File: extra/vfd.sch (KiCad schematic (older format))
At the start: 47 parts, among them P10 GU128x64E-U100, P11 gui140x16j-7002, P12 digital_in, P13 digital_out, U3 74LS125, U4 74LS125, U5 74LS125, U6 74LS125, U7 74LS125, U8 74LS245-xnor

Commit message: working with enables on extra board
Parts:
- added R? (x3): PULL, xnorman:Resistor_Horizontal_RM10mm-xnorman, symbol R
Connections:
- net 3.3v: now also R?.1
- net GND: no longer U3.1 (E), U3.10 (E), U3.13 (E), U3.4 (E), U4.1 (E), U4.10 (E), U4.4 (E), U5.1 (E), U5.10 (E), U5.13 (E), U5.4 (E), U7.13 (E), U8.19 (CE)
- net VCC: now also R?.2, R?.2
- net bb-vfdD7enable renamed bb-vfdDOUTenable
- net bb-vfdDOUTenable: now also U3.1 (E), U3.10 (E), U3.13 (E), U3.4 (E), U4.1 (E), U4.10 (E), U4.4 (E), R?.1
- new net bb-digitalOutEnable: U8.19 (CE)
- new net bb-vfdCTRLenable: R?.1, U5.1 (E), U5.10 (E), U5.13 (E), U5.4 (E), U7.13 (E)
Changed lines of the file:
@@
 $Descr A4 11693 8268
 encoding utf-8
-Sheet 3 2
+Sheet 2 2
 Title ""
 Date ""
@@
 $EndComp
 Text GLabel 1250 7650 0    60   Input ~ 0
-bb-vfdD7enable
+bb-vfdDOUTenable
 $Comp
 L 74LS125 U5
@@
 Wire Wire Line
 	1750 1250 2200 1250
-Connection ~ 2050 1250
 Wire Wire Line
 	1250 850  1150 850
@@
 	2150 7250 2350 7250
 Wire Wire Line
-	1350 3600 1700 3600
-Wire Wire Line
-	1350 4150 1700 4150
-Wire Wire Line
-	1350 4750 1700 4750
-Wire Wire Line
-	1350 5250 1700 5250
-Wire Wire Line
-	1350 5900 1700 5900
-Wire Wire Line
-	1350 6450 1700 6450
-Wire Wire Line
-	1350 7050 1700 7050
-Wire Wire Line
-	1250 7650 1700 7650
-Wire Wire Line
 	1700 7650 1700 7550
 Wire Wire Line
@@
 	6050 4850 6250 4850
 Wire Wire Line
-	5200 3500 5600 3500
-Wire Wire Line
-	5200 4050 5600 4050
-Wire Wire Line
-	5200 4650 5600 4650
-Wire Wire Line
-	5200 5150 5600 5150
-Wire Wire Line
 	6250 5500 6050 5500
 Wire Wire Line
@@
 	8700 2000 8950 2000
 Wire Wire Line
-	8950 2300 8850 2300
+	8750 2300 8950 2300
 Wire Wire Line
 	8150 2450 9650 2450
@@
 Wire Wire Line
 	1500 3450 1550 3450
-Connection ~ 1500 3600
 Wire Wire Line
 	1500 4150 1500 4000
 Wire Wire Line
 	1500 4000 1550 4000
-Connection ~ 1500 4150
 Wire Wire Line
 	1500 4750 1500 4600
 Wire Wire Line
 	1500 4600 1550 4600
-Connection ~ 1500 4750
 Wire Wire Line
 	1500 5250 1500 5100
 Wire Wire Line
 	1500 5100 1550 5100
-Connection ~ 1500 5250
 Wire Wire Line
 	1500 5900 1500 5750
 Wire Wire Line
 	1500 5750 1550 5750
-Connection ~ 1500 5900
 Wire Wire Line
 	1500 6450 1500 6300
 Wire Wire Line
 	1500 6300 1550 6300
-Connection ~ 1500 6450
 Wire Wire Line
 	1500 6900 1500 7400
 Wire Wire Line
 	1500 6900 1550 6900
-Connection ~ 1500 7050
 Wire Wire Line
 	1500 7400 1550 7400
@@
 Connection ~ 1400 6600
 Wire Wire Line
-	5400 3500 5400 3350
-Wire Wire Line
 	5400 3350 5450 3350
-Connection ~ 5400 3500
 Wire Wire Line
 	5400 4050 5400 3900
 Wire Wire Line
 	5400 3900 5450 3900
-Connection ~ 5400 4050
 Wire Wire Line
 	5400 4650 5400 4500
 Wire Wire Line
 	5400 4500 5450 4500
-Connection ~ 5400 4650
 Wire Wire Line
 	5400 5150 5400 5000
 Wire Wire Line
 	5400 5000 5450 5000
-Connection ~ 5400 5150
 Wire Wire Line
 	5400 5800 5400 5650
@@
 	8800 5950 9200 5950
 Wire Wire Line
-	8800 6450 9200 6450
+	8800 6450 9000 6450
 Wire Wire Line
 	8550 4500 8750 4500
@@
 Wire Wire Line
 	9000 6300 9050 6300
-Connection ~ 9000 6450
 Wire Wire Line
 	8950 6000 9050 6000
@@
 Wire Wire Line
 	4900 2300 5400 2300
-Connection ~ 8850 2300
 $Comp
 L CONN_01X07 P12
@@
 	8150 1900 8150 2450
 Wire Wire Line
-	8850 2300 8850 2450
-Connection ~ 8850 2450
-Wire Wire Line
 	9650 1050 9650 1250
 NoConn ~ 10350 1900
@@
 Wire Wire Line
 	9450 2850 9450 3150
+Wire Wire Line
+	1500 3600 1350 3600
+Wire Wire Line
+	1500 4150 1350 4150
+Wire Wire Line
+	1500 4750 1350 4750
+Wire Wire Line
+	1500 5250 1350 5250
+Wire Wire Line
+	1500 7050 1350 7050
+Connection ~ 1500 7050
+Wire Wire Line
+	1500 6450 1350 6450
+Wire Wire Line
+	1500 5900 1350 5900
+Wire Wire Line
+	1700 3600 2200 3600
+Wire Wire Line
+	2200 3600 2200 7650
+Wire Wire Line
+	2200 4150 1700 4150
+Wire Wire Line
+	2200 4750 1700 4750
+Connection ~ 2200 4150
+Wire Wire Line
+	2200 5250 1700 5250
+Connection ~ 2200 4750
+Wire Wire Line
+	2200 5900 1700 5900
+Connection ~ 2200 5250
+Wire Wire Line
+	2200 6450 1700 6450
+Connection ~ 2200 5900
+Wire Wire Line
+	2200 7050 1700 7050
+Connection ~ 2200 6450
+Wire Wire Line
+	2200 7650 1250 7650
+Connection ~ 2200 7050
+Connection ~ 1700 7650
+Wire Wire Line
+	5400 3500 5400 3350
+Wire Wire Line
+	5400 3500 5200 3500
+Wire Wire Line
+	5400 4050 5200 4050
+Wire Wire Line
+	5400 4650 5200 4650
+Wire Wire Line
+	5400 5150 5200 5150
+Wire Wire Line
+	5600 3500 6100 3500
+Wire Wire Line
+	6100 3500 6100 5150
+Wire Wire Line
+	6100 4050 5600 4050
+Wire Wire Line
+	6100 4650 5600 4650
+Connection ~ 6100 4050
+Wire Wire Line
+	5600 5150 6350 5150
+Connection ~ 6100 4650
+Text GLabel 6350 5150 2    60   Input ~ 0
+bb-vfdCTRLenable
+Connection ~ 6100 5150
+Text GLabel 9350 6450 2    60   Input ~ 0
+bb-vfdCTRLenable
+Wire Wire Line
+	9350 6450 9200 6450
+Text GLabel 8700 2350 0    60   Input ~ 0
+bb-digitalOutEnable
+Wire Wire Line
+	8700 2350 8750 2350
+Wire Wire Line
+	8750 2350 8750 2300
+$Comp
+L R R?
+U 1 1 589BE25B
+P 8900 2450
+F 0 "R?" V 8980 2450 50  0000 C CNN
+F 1 "PULL" V 8900 2450 50  0000 C CNN
+F 2 "xnorman:Resistor_Horizontal_RM10mm-xnorman" V 8830 2450 50  0001 C CNN
+F 3 "" H 8900 2450 50  0000 C CNN
+	1    8900 2450
+	-1   0    0    1
+$EndComp
+Text GLabel 8850 2600 0    60   Input ~ 0
+3.3v
+Wire Wire Line
+	8900 2600 8850 2600
+$Comp
+L R R?
+U 1 1 589BE85D
+P 2500 6550
+F 0 "R?" V 2580 6550 50  0000 C CNN
+F 1 "PULL" V 2500 6550 50  0000 C CNN
+F 2 "xnorman:Resistor_Horizontal_RM10mm-xnorman" V 2430 6550 50  0001 C CNN
+F 3 "" H 2500 6550 50  0000 C CNN
+	1    2500 6550
+	0    -1   -1   0
+$EndComp
+Text GLabel 2800 6550 2    60   Input ~ 0
+5v
+Wire Wire Line
+	2800 6550 2650 6550
+Wire Wire Line
+	2350 6550 2200 6550
+Connection ~ 2200 6550
+$Comp
+L R R?
+U 1 1 589BFAF3
+P 6800 5000
+F 0 "R?" V 6880 5000 50  0000 C CNN
+F 1 "PULL" V 6800 5000 50  0000 C CNN
+F 2 "xnorman:Resistor_Horizontal_RM10mm-xnorman" V 6730 5000 50  0001 C CNN
+F 3 "" H 6800 5000 50  0000 C CNN
+	1    6800 5000
+	0    -1   -1   0
+$EndComp
+Text GLabel 7150 5000 2    60   Input ~ 0
+5v
+Wire Wire Line
+	6650 5000 6100 5000
+Connection ~ 6100 5000
+Wire Wire Line
+	6950 5000 7150 5000
 $EndSCHEMATC

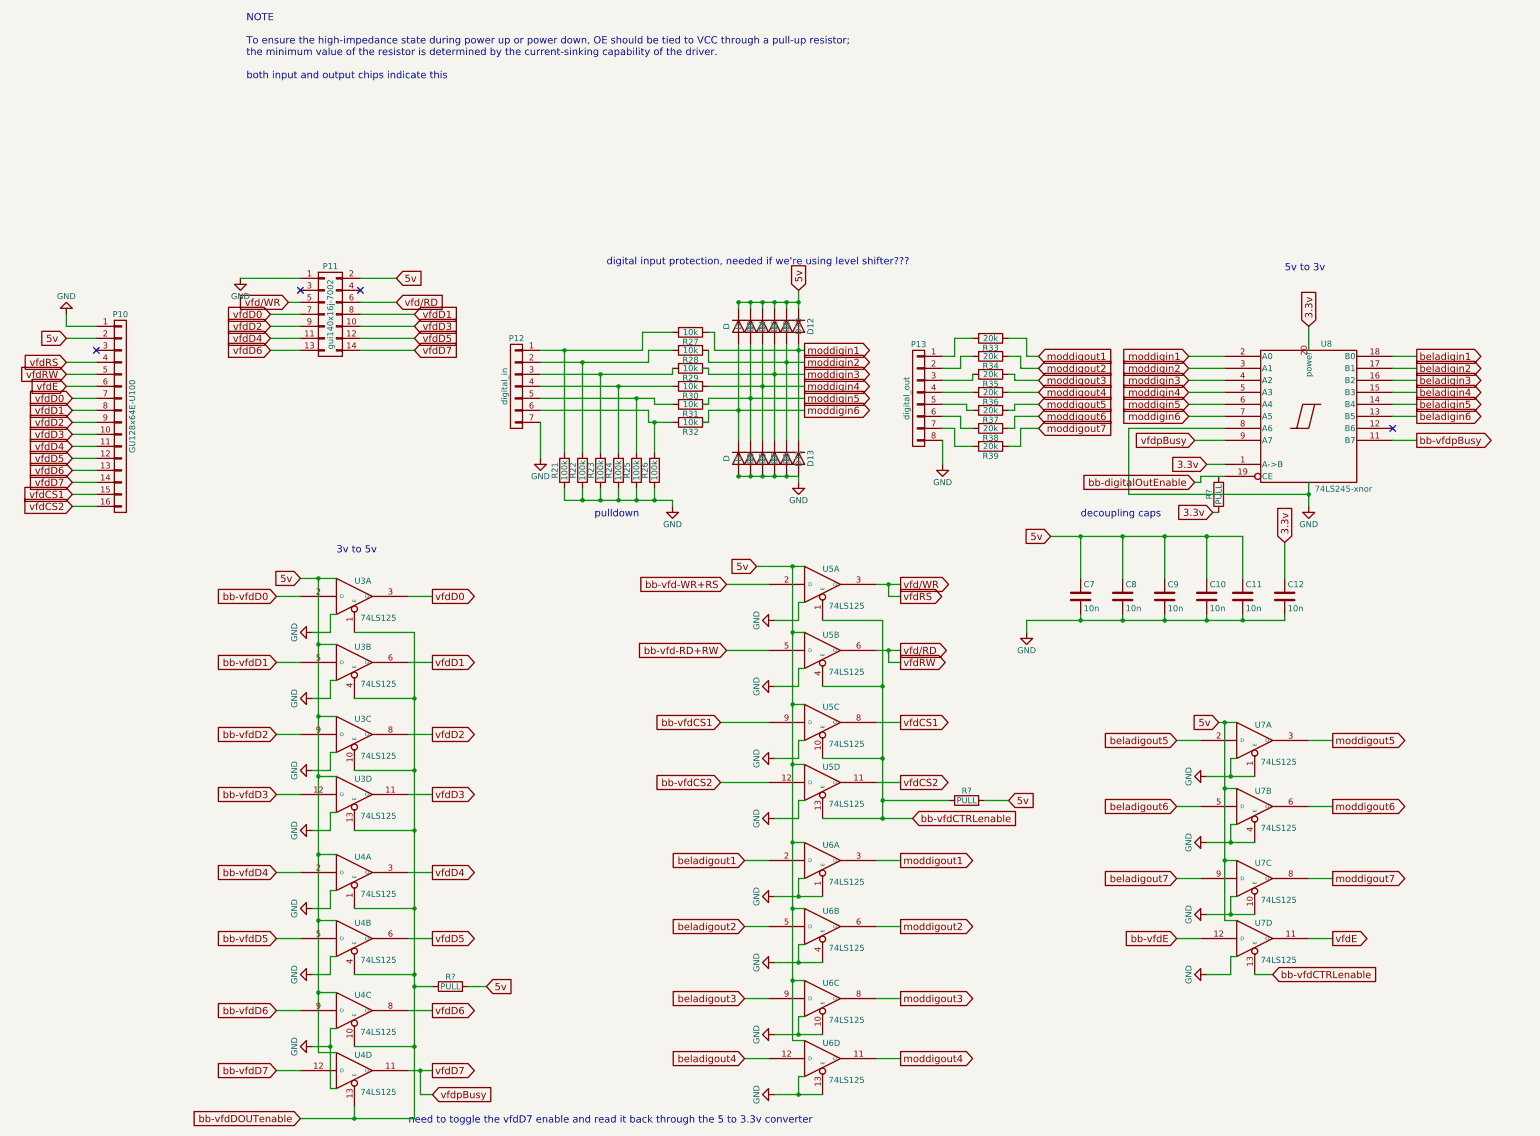
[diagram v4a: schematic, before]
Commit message: ditched power, remapped a bunch of io
should have all the emmc and lcd lines disabled at boot
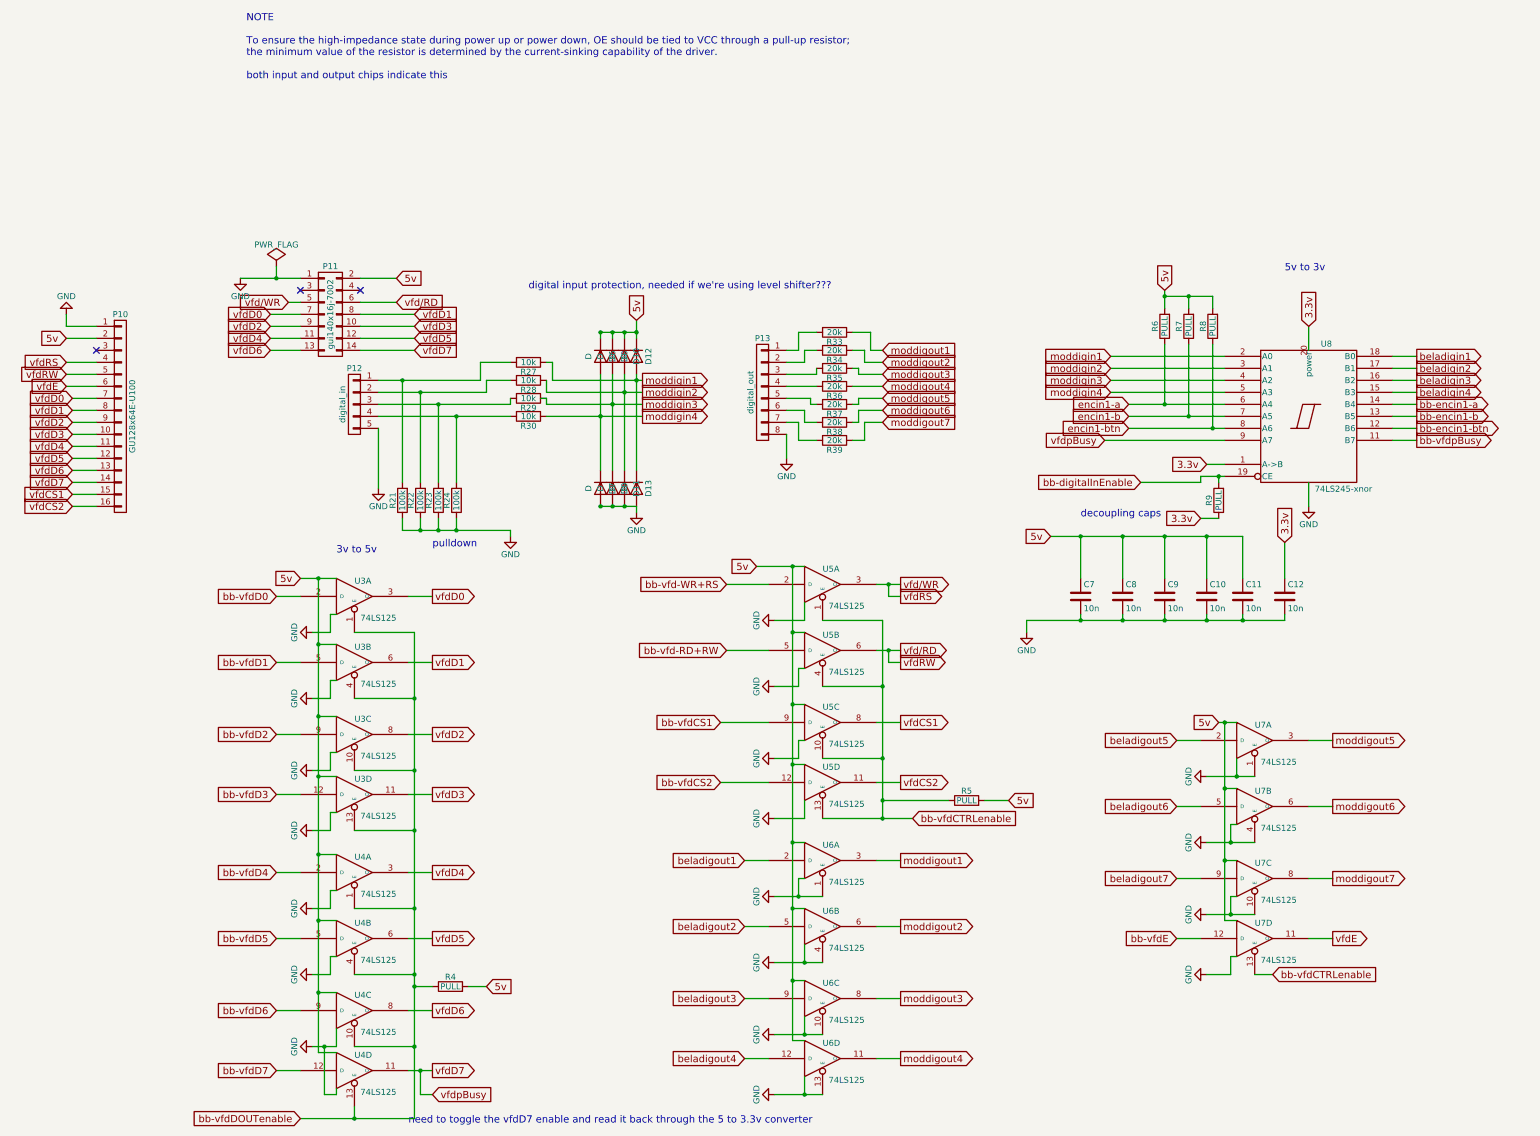
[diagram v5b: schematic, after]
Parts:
- removed D2, D3, D4, D5: D, Diodes_ThroughHole:Diode_DO-41_SOD81_Horizontal_RM10, symbol D
- removed P12: digital_in, Pin_Headers:Pin_Header_Straight_1x07_Pitch2.54mm, symbol CONN_01X07
- removed R25, R26: 100k, xnorman:Resistor_Horizontal_RM10mm-xnorman, symbol R
- removed R31, R32: 10k, xnorman:Resistor_Horizontal_RM10mm-xnorman, symbol R
- added P12: digital_in, Pin_Headers:Pin_Header_Straight_1x05_Pitch2.54mm, symbol CONN_01X05
- added R6, R7, R8: PULL, xnorman:Resistor_Horizontal_RM10mm-xnorman, symbol R
- D10, D11, D12, D13, D6, D7, D8, D9: footprint Diodes_ThroughHole:Diode_DO-41_SOD81_Horizontal_RM10 -> Diodes_ThroughHole:D_DO-41_SOD81_P7.62mm_Horizontal
- gave numbers to parts that had none: 3
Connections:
- net bb-digitalOutEnable is gone; now on net bb-digitalInEnable: U8.19 (CE)
- net GND: now also P12.5 (P5); no longer U8.8 (A6)
- net VCC: now also R6.2, R7.2, R8.2
- net at R21.2, R27.2: now also P12.1 (P1)
- net at R22.2, R28.2: now also P12.2 (P2)
- net at R23.2, R29.2: now also P12.3 (P3)
- net at R24.2, R30.2: now also P12.4 (P4)
- net bb-encin1-btn: now reaches U8.12 (B6)
- net bb-digitalInEnable: now reaches R9.2
- net beladigin5 renamed bb-encin1-a
- net beladigin6 renamed bb-encin1-b
- net moddigin5 renamed encin1-a
- net encin1-a: now also R6.1
- net moddigin6 renamed encin1-b
- net encin1-b: now also R7.1
- new net encin1-btn: R8.1, U8.8 (A6)
- no-connect marks 4 -> 3
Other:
- moved on the sheet: D10, D11, D12, D13, D6, D7, D8, D9, P13, R21, R22, R23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
